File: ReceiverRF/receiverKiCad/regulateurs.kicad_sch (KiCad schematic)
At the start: 15 parts, among them SW5 SW_SPST, U2 NCV5501DT33RKG, U3 NJM2882F05-TE1

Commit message: changement switch pour switch plus petite
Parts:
- SW5: footprint Footprints:D102J12S215PQA_CNK -> Footprints:SW_1MS02Q_CNK
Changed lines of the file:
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@@
 			)
 		)
-		(property "Footprint" "Footprints:D102J12S215PQA_CNK"
+		(property "Footprint" "Footprints:SW_1MS02Q_CNK"
 			(at 53.34 33.02 0)
 			(effects
@@
 			)
 		)
-		(property "Datasheet" "https://www.digikey.ca/en/products/detail/c-k/D102J12S215PQA/768267"
+		(property "Datasheet" "https://www.digikey.ca/en/products/detail/c-k/L101011MS02Q/484142"
 			(at 53.34 33.02 0)
 			(effects

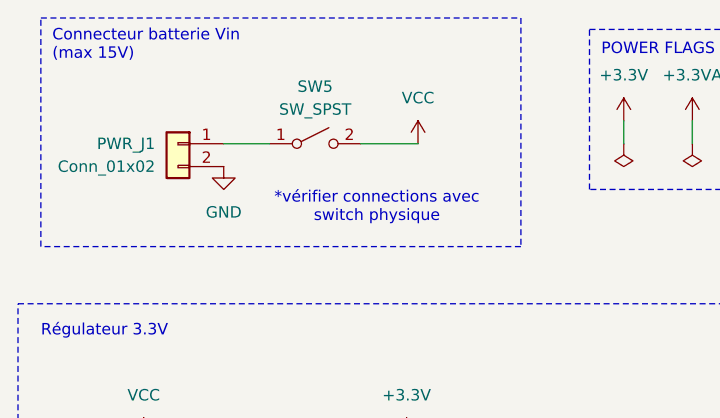
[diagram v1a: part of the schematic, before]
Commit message: changement circuit volume du buzzer. Ajustement du volume direct plutot que software.
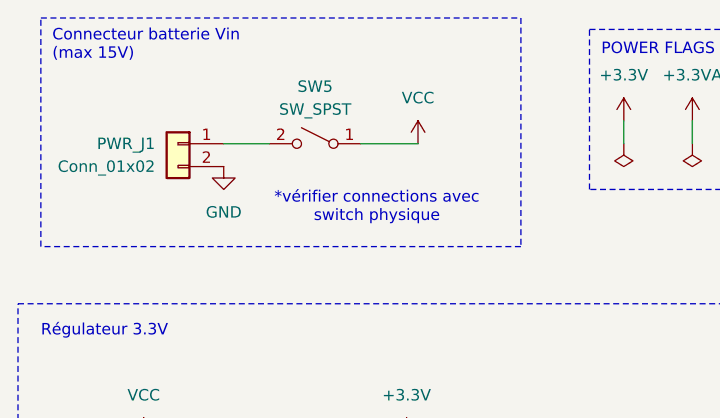
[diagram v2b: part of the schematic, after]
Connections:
- net VCC: now also SW5.1 (A); no longer SW5.2 (B)
- net at PWR_J1.1 (Pin_1): now also SW5.2 (B); no longer SW5.1 (A)
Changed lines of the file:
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@@
+	(wire
+		(pts
+			(xy 58.42 33.02) (xy 64.77 33.02)
+		)
+		(stroke
+			(width 0)
+			(type default)
+		)
+	)
 	(wire
 		(pts
@@
 	(wire
 		(pts
-			(xy 58.42 33.02) (xy 64.77 33.02)
-		)
-		(stroke
-			(width 0)
-			(type default)
-		)
-	)
-	(wire
-		(pts
 			(xy 63.5 68.58) (xy 63.5 66.04)
 		)
@@
 	(wire
 		(pts
+			(xy 43.18 33.02) (xy 48.26 33.02)
+		)
+		(stroke
+			(width 0)
+			(type default)
+		)
+	)
+	(wire
+		(pts
 			(xy 63.5 68.58) (xy 63.5 69.85)
 		)
@@
 		(pts
 			(xy 190.5 87.63) (xy 190.5 92.71)
-		)
-		(stroke
-			(width 0)
-			(type default)
-		)
-	)
-	(wire
-		(pts
-			(xy 43.18 33.02) (xy 48.26 33.02)
 		)
 		(stroke
@@
 		(lib_id "Switch:SW_SPST")
 		(at 53.34 33.02 0)
+		(mirror y)
 		(unit 1)
 		(exclude_from_sim no)
@@
 		(on_board yes)
 		(dnp no)
-		(fields_autoplaced yes)
 		(property "Reference" "SW5"
 			(at 53.34 26.67 0)
